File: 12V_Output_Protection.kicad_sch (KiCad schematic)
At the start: 6 parts, among them U16 VND7050AJTR

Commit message: All the diodes, and other layout work
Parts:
- D30: footprint Diode_SMD:D_0805_2012Metric -> Diode_SMD:D_SOD-123; LCSC (none) -> C83152; MPN (none) -> BAT46W-7-F; Manufacturer (none) -> Diodes Incorporated
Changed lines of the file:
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@@
 			)
 		)
-		(property "Footprint" "Diode_SMD:D_0805_2012Metric"
+		(property "Footprint" "Diode_SMD:D_SOD-123"
 			(at 130.81 148.59 0)
 			(effects
@@
 			)
 		)
-		(property "Datasheet" "~"
+		(property "Datasheet" "https://www.lcsc.com/datasheet/lcsc_datasheet_2412251151_Diodes-Incorporated-BAT46W-7-F_C83152.pdf"
 			(at 130.81 148.59 0)
 			(effects
@@
 			)
 		)
+		(property "LCSC" "C83152"
+			(at 130.81 148.59 0)
+			(effects
+				(font
+					(size 1.27 1.27)
+				)
+			)
+		)
+		(property "MPN" "BAT46W-7-F"
+			(at 130.81 148.59 0)
+			(effects
+				(font
+					(size 1.27 1.27)
+				)
+			)
+		)
+		(property "Manufacturer" "Diodes Incorporated"
+			(at 130.81 148.59 0)
+			(effects
+				(font
+					(size 1.27 1.27)
+				)
+			)
+		)

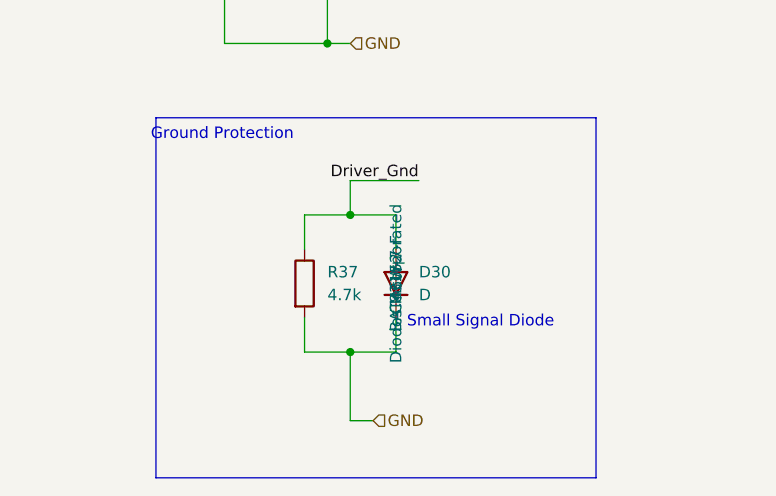
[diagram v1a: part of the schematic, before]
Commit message: Layout, smaller resistors and HB + Error LEDs
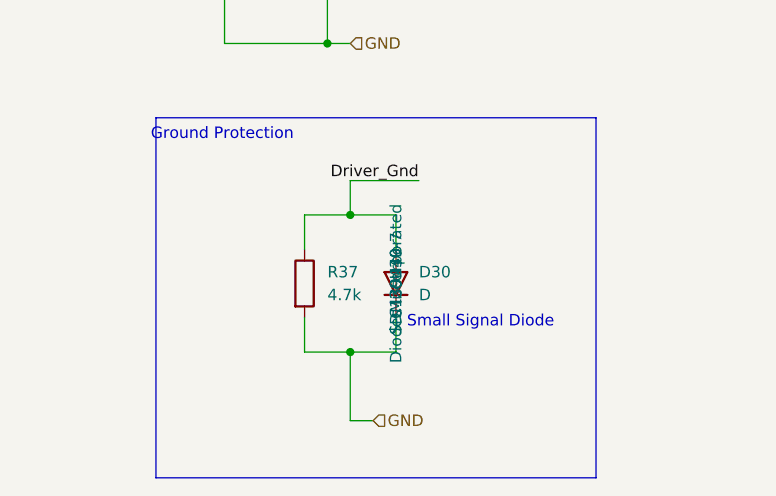
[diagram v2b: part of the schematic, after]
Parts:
- D30: footprint Diode_SMD:D_SOD-123 -> Diode_SMD:D_SOD-523; LCSC C83152 -> C139439; MPN BAT46W-7-F -> SDM20U40-7
- R38, R39: footprint Resistor_SMD:R_0603_1608Metric -> Resistor_SMD:R_0402_1005Metric; LCSC (none) -> C25756
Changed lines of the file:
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@@
 			)
 		)
-		(property "Footprint" "Resistor_SMD:R_0603_1608Metric"
+		(property "Footprint" "Resistor_SMD:R_0402_1005Metric"
 			(at 115.57 89.662 90)
 			(effects
@@
 			)
 		)
-		(property "LCSC" ""
+		(property "LCSC" "C25756"
 			(at 115.57 91.44 0)
 			(effects
@@
 			)
 		)
-		(property "Footprint" "Diode_SMD:D_SOD-123"
-			(at 130.81 148.59 0)
-			(effects
-				(font
-					(size 1.27 1.27)
-				)
-				(hide yes)
-			)
-		)
-		(property "Datasheet" "https://www.lcsc.com/datasheet/lcsc_datasheet_2412251151_Diodes-Incorporated-BAT46W-7-F_C83152.pdf"
+		(property "Footprint" "Diode_SMD:D_SOD-523"
+			(at 130.81 148.59 0)
+			(effects
+				(font
+					(size 1.27 1.27)
+				)
+				(hide yes)
+			)
+		)
+		(property "Datasheet" "https://www.lcsc.com/datasheet/lcsc_datasheet_2412251002_Diodes-Incorporated-SDM20U40-7_C139439.pdf"
 			(at 130.81 148.59 0)
 			(effects
@@
 			)
 		)
-		(property "LCSC" "C83152"
-			(at 130.81 148.59 0)
-			(effects
-				(font
-					(size 1.27 1.27)
-				)
-			)
-		)
-		(property "MPN" "BAT46W-7-F"
+		(property "LCSC" "C139439"
+			(at 130.81 148.59 0)
+			(effects
+				(font
+					(size 1.27 1.27)
+				)
+			)
+		)
+		(property "MPN" "SDM20U40-7"
 			(at 130.81 148.59 0)
 			(effects
@@
 			)
 		)
-		(property "Footprint" "Resistor_SMD:R_0603_1608Metric"
+		(property "Footprint" "Resistor_SMD:R_0402_1005Metric"
 			(at 115.57 87.122 90)
 			(effects
@@
 			)
 		)
-		(property "LCSC" ""
+		(property "LCSC" "C25756"
 			(at 115.57 88.9 0)
 			(effects

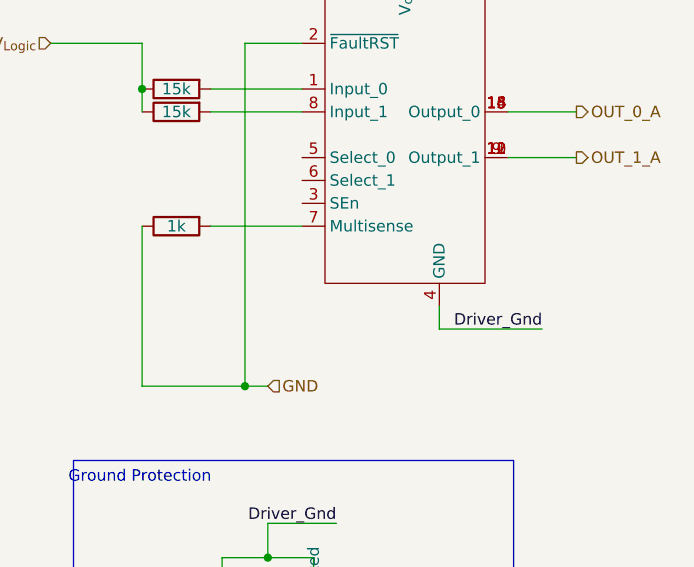
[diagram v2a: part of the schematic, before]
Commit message: Finalised RS485 Circuit, Layout improvemnts, mounting holes, silkscreen...
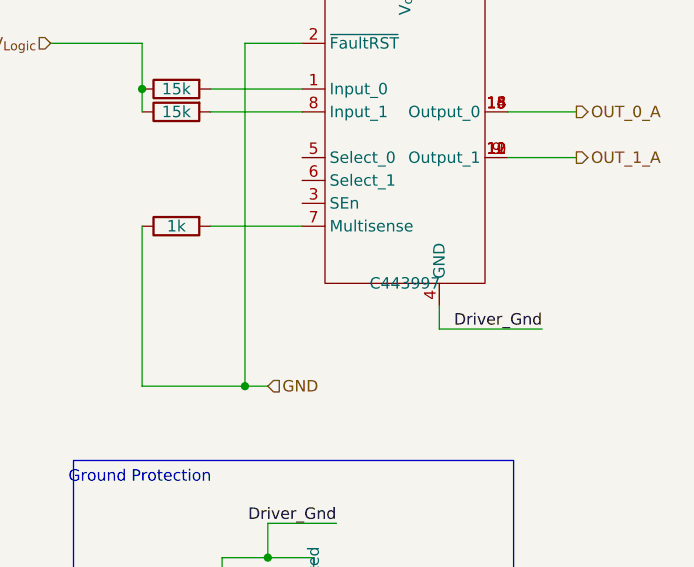
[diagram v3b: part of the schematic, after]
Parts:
- U16: LCSC (none) -> C443997
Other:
- company: (none) -> eChook
- title: (none) -> BMS Comms Master Board
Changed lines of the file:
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@@
 	(generator_version "9.0")
 	(paper "A4")
+	(title_block
+		(title "BMS Comms Master Board")
+		(date "2025-05-21")
+		(rev "0.1")
+		(company "eChook")
+	)
 	(rectangle
 		(start 104.14 130.175)
@@
 			)
 		)
+		(property "LCSC" "C443997"
+			(at 140.97 110.49 0)
+			(effects
+				(font
+					(size 1.27 1.27)
+				)
+			)
+		)

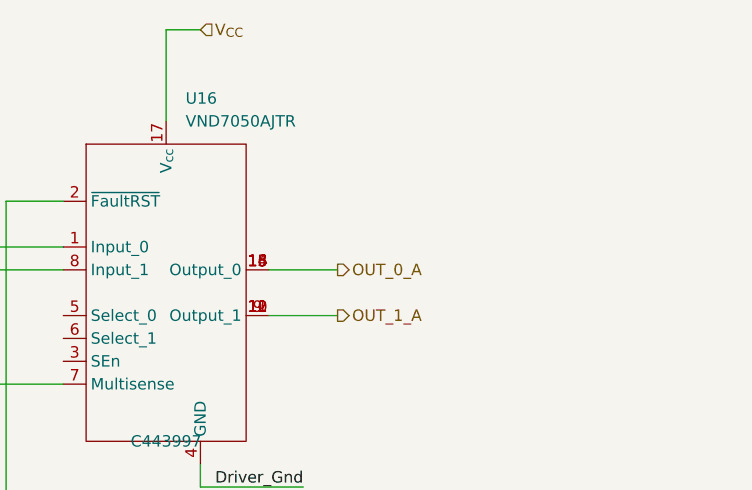
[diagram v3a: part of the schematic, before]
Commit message: added 12v Feed Error LEDs
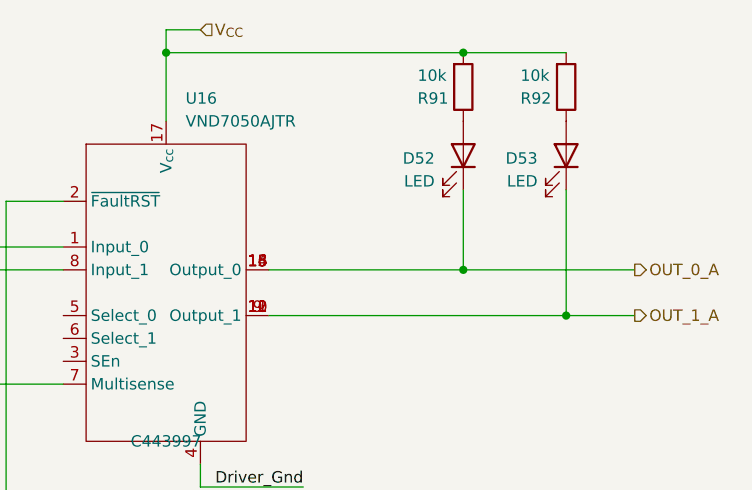
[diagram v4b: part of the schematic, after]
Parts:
- added D52, D53: LED, LED_SMD:LED_0603_1608Metric, symbol Device:LED
- added R91, R92: 10k, Resistor_SMD:R_0603_1608Metric, symbol Device:R
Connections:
- net OUT_0_A: now also D52.1 (K)
- net OUT_1_A: now also D53.1 (K)
- net V_{CC}: now also R91.2, R92.2
- new net: D52.2 (A), R91.1
- new net: D53.2 (A), R92.1
